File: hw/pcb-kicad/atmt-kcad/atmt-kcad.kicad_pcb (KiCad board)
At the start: 2 copper layers, 14 parts, among them J3 Conn_01x04_Male, J4 Conn_01x04_Male, U1 ESP32-WROOM-32U, U2 LP2987-3.3_SOIC8_VSSOP8, U3 4504, U4 L293

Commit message: Before refactoring
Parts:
- added C7: 100n, Capacitor_SMD:C_0805_2012Metric_Pad1.18x1.45mm_HandSolder, B.Cu at (101.2, 111.1)
- added D2: PowerOn, LED_THT:LED_D3.0mm, F.Cu at (94.7, 74.8)
- added J1: Reset, Connector_PinHeader_2.54mm:PinHeader_1x02_P2.54mm_Vertical, F.Cu at (111.2, 68.4)
- added J10: JTAG, Connector_PinHeader_2.54mm:PinHeader_1x04_P2.54mm_Vertical, F.Cu at (119.6, 68.4)
- added J11: BAT+, Connector_Wire:SolderWire-1.5sqmm_1x01_D1.7mm_OD3mm, F.Cu at (95.6, 106.4)
- added J12: BAT-, Connector_Wire:SolderWire-1.5sqmm_1x01_D1.7mm_OD3mm, F.Cu at (145.4, 72.8)
- added J13: Steering, Connector_Phoenix_MSTB:PhoenixContact_MSTBA_2,5_2-G-5,08_1x02_P5.08mm_Horizontal, F.Cu at (138.7, 75.6)
- added J14: Motor, Connector_Phoenix_MSTB:PhoenixContact_MSTBA_2,5_2-G-5,08_1x02_P5.08mm_Horizontal, F.Cu at (138.9, 116.4)
- added J15: BOOT, Connector_PinHeader_2.54mm:PinHeader_1x02_P2.54mm_Vertical, F.Cu at (111.2, 63.2)
- added J16: Light, Connector_PinHeader_2.54mm:PinHeader_1x03_P2.54mm_Vertical, F.Cu at (103.0, 82.0)
- added J17: Buck/Boost, Connector_PinHeader_2.54mm:PinHeader_1x03_P2.54mm_Vertical, F.Cu at (106.5, 119.5)
- added J2: PowerSw, Connector_PinHeader_2.54mm:PinHeader_1x02_P2.54mm_Vertical, F.Cu at (95.2, 112.4)
- added J5: US-Right, Connector_PinHeader_2.54mm:PinHeader_1x04_P2.54mm_Vertical, F.Cu at (144.8, 89.8)
- added J6: US-Left, Connector_PinHeader_2.54mm:PinHeader_1x04_P2.54mm_Vertical, F.Cu at (95.4, 89.8)
- added J7: I2Cx2, Connector_PinHeader_2.54mm:PinHeader_1x04_P2.54mm_Vertical, F.Cu at (119.5, 78.2)
- added J8: PRG, Connector_PinHeader_2.54mm:PinHeader_1x04_P2.54mm_Vertical, F.Cu at (119.5, 63.2)
- added J9: I2C_1, Connector_PinHeader_2.54mm:PinHeader_1x04_P2.54mm_Vertical, F.Cu at (119.5, 74.4)
- added R2: 10k, Resistor_SMD:R_0805_2012Metric_Pad1.20x1.40mm_HandSolder, B.Cu at (109.1, 87.3)
- added R3: 470k, Resistor_SMD:R_0805_2012Metric_Pad1.20x1.40mm_HandSolder, B.Cu at (101.1, 107.0)
- added R4: 100k, Resistor_SMD:R_0805_2012Metric_Pad1.20x1.40mm_HandSolder, B.Cu at (101.3, 115.1)
- added R5: 10k, Resistor_SMD:R_0805_2012Metric_Pad1.20x1.40mm_HandSolder, B.Cu at (121.0, 81.6)
- added R6: 10k, Resistor_SMD:R_0805_2012Metric_Pad1.20x1.40mm_HandSolder, B.Cu at (120.9, 85.1)
- added R7: 470, Resistor_SMD:R_0805_2012Metric_Pad1.20x1.40mm_HandSolder, B.Cu at (95.8, 78.4)
- C1, C4: value C -> 10u; moved to B.Cu
- C2: value C_Polarized -> 100n; footprint Capacitor_THT:CP_Axial_L11.0mm_D6.0mm_P18.00mm_Horizontal -> Capacitor_SMD:C_0805_2012Metric_Pad1.18x1.45mm_HandSolder; moved to B.Cu
- C3: value C -> 100n; moved to B.Cu
- C5: value C -> 1u; moved to B.Cu
- C6: value C_Polarized -> 22u
- D1, U3: moved to B.Cu
- J3: value Conn_01x04_Male -> US-Front
- J4: value Conn_01x04_Male -> US-Rear
- R1: value R -> 330k; moved to B.Cu
- U2: value LP2987-3.3_SOIC8_VSSOP8 -> LP2987-3.3; moved to B.Cu
- U4: value L293 -> L293DD; footprint Package_DIP:DIP-16_W7.62mm_SMDSocket_SmallPads -> MyFootprints:SO-20_STM; moved to B.Cu
- moved J3 171.7 mm to (101.4, 74.0), turned to 90 degrees
- moved J4 159.3 mm to (119.8, 119.6), turned to 90 degrees
- moved U4 107.8 mm to (135.1, 89.5), turned to 180 degrees
- moved C6 105.9 mm to (94.8, 82.4)
- moved U3 97.6 mm to (137.6, 105.9), turned to 180 degrees
- moved C2 90.8 mm to (112.6, 72.2)
- moved C4 90.8 mm to (108.7, 116.8)
- moved R1 75.9 mm to (105.0, 110.5), turned to -90 degrees
- moved C3 74.2 mm to (116.5, 87.7), turned to 90 degrees
- moved C1 72.1 mm to (114.1, 117.0), turned to 180 degrees
- moved C5 72.0 mm to (109.2, 91.4)
- moved U2 65.0 mm to (111.0, 110.6), turned to 180 degrees
- moved D1 33.4 mm to (111.1, 101.5)
- moved U1 17.0 mm to (121.8, 95.2)
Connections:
- C1 pad 1: unconnected-(C1-Pad1) -> GND
- C1 pad 2: unconnected-(C1-Pad2) -> B+
- C2 pad 1: unconnected-(C2-Pad1) -> /EN
- C2 pad 2: unconnected-(C2-Pad2) -> GND
- C3 pad 1: unconnected-(C3-Pad1) -> 3V3
- C3 pad 2: unconnected-(C3-Pad2) -> GND
- C4 pad 1: unconnected-(C4-Pad1) -> GND
- C4 pad 2: unconnected-(C4-Pad2) -> 3V3
- C5 pad 1: unconnected-(C5-Pad1) -> /EN
- C5 pad 2: unconnected-(C5-Pad2) -> GND
- C6 pad 1: unconnected-(C6-Pad1) -> 3V3
- C6 pad 2: unconnected-(C6-Pad2) -> GND
- D1 pad 1: unconnected-(D1-Pad1) -> Net-(D1-K)
- D1 pad 2: unconnected-(D1-Pad2) -> 3V3
- J3 pad 1: unconnected-(J3-Pad1) -> /5V
- J3 pad 2: unconnected-(J3-Pad2) -> /Trig1
- J3 pad 3: unconnected-(J3-Pad3) -> /Echo1
- J3 pad 4: unconnected-(J3-Pad4) -> GND
- J4 pad 1: unconnected-(J4-Pad1) -> /5V
- J4 pad 2: unconnected-(J4-Pad2) -> /Trig4
- J4 pad 3: unconnected-(J4-Pad3) -> /Echo4
- J4 pad 4: unconnected-(J4-Pad4) -> GND
- R1 pad 1: unconnected-(R1-Pad1) -> Net-(U2-~{ERROR})
- R1 pad 2: unconnected-(R1-Pad2) -> 3V3
- U1 pad 1: Net-(U1-Pad1) -> GND
- U1 pad 10: unconnected-(U1-Pad10) -> /Echo3L
- U1 pad 11: unconnected-(U1-Pad11) -> /Trig3
- U1 pad 12: unconnected-(U1-Pad12) -> /M2F
- U1 pad 13: unconnected-(U1-Pad13) -> /TMS
- U1 pad 14: unconnected-(U1-Pad14) -> /TDI
- U1 pad 15: Net-(U1-Pad1) -> GND
- U1 pad 16: unconnected-(U1-Pad16) -> /TCK
- U1 pad 2: unconnected-(U1-Pad2) -> 3V3
- U1 pad 23: unconnected-(U1-Pad23) -> /TDO
- U1 pad 24: unconnected-(U1-Pad24) -> /M1E
- U1 pad 25: unconnected-(U1-Pad25) -> /IO0
- U1 pad 26: unconnected-(U1-Pad26) -> /M1F
- U1 pad 27: unconnected-(U1-Pad27) -> /Trig1
- U1 pad 28: unconnected-(U1-Pad28) -> /Trig2
- U1 pad 29: unconnected-(U1-Pad29) -> /M1R
- U1 pad 3: unconnected-(U1-Pad3) -> /EN
- U1 pad 30: unconnected-(U1-Pad30) -> /Echo4L
- U1 pad 31: unconnected-(U1-Pad31) -> /Trig4
- U1 pad 33: unconnected-(U1-Pad33) -> /SDA
- U1 pad 34: unconnected-(U1-Pad34) -> /RX
- U1 pad 35: unconnected-(U1-Pad35) -> /TX
- U1 pad 36: unconnected-(U1-Pad36) -> /SCL
- U1 pad 37: unconnected-(U1-Pad37) -> /M2R
- U1 pad 38: Net-(U1-Pad1) -> GND
- U1 pad 39: Net-(U1-Pad1) -> GND
- U1 pad 6: unconnected-(U1-Pad6) -> /Echo1L
- U1 pad 7: unconnected-(U1-Pad7) -> /Echo2L
- U1 pad 8: unconnected-(U1-Pad8) -> /L1
- U1 pad 9: unconnected-(U1-Pad9) -> /M2E
- U2 pad 3: unconnected-(U2-Pad3) -> GND
- U2 pad 4: unconnected-(U2-Pad4) -> B+
- U2 pad 5: unconnected-(U2-Pad5) -> 3V3
- U2 pad 6: unconnected-(U2-Pad6) -> 3V3
- U2 pad 7: unconnected-(U2-Pad7) -> Net-(U2-~{ERROR})
- U2 pad 8: unconnected-(U2-Pad8) -> Net-(D1-K)
- U3 pad 1: unconnected-(U3-Pad1) -> /5V
- U3 pad 10: unconnected-(U3-Pad10) -> /Echo4L
- U3 pad 13: unconnected-(U3-Pad13) -> /5V
- U3 pad 16: unconnected-(U3-Pad16) -> 3V3
- U3 pad 2: unconnected-(U3-Pad2) -> /Echo1L
- U3 pad 3: unconnected-(U3-Pad3) -> /Echo1
- U3 pad 4: unconnected-(U3-Pad4) -> /Echo2L
- U3 pad 5: unconnected-(U3-Pad5) -> /Echo2
- U3 pad 6: unconnected-(U3-Pad6) -> /Echo3L
- U3 pad 7: unconnected-(U3-Pad7) -> /Echo3
- U3 pad 8: unconnected-(U3-Pad8) -> GND
- U3 pad 9: unconnected-(U3-Pad9) -> /Echo4
- U4 pad 1: unconnected-(U4-Pad1) -> /M1E
- U4 pad 10: unconnected-(U4-Pad10) -> /5V
- U4 pad 11: unconnected-(U4-Pad11) -> /M2E
- U4 pad 12: unconnected-(U4-Pad12) -> /M2F
- U4 pad 13: unconnected-(U4-Pad13) -> /M2_2
- U4 pad 14: unconnected-(U4-Pad14) -> GND
- U4 pad 15: unconnected-(U4-Pad15) -> GND
- U4 pad 16: unconnected-(U4-Pad16) -> GND
- U4 pad 2: unconnected-(U4-Pad2) -> /M1F
- U4 pad 3: unconnected-(U4-Pad3) -> /M1_1
- U4 pad 4: unconnected-(U4-Pad4) -> GND
- U4 pad 5: unconnected-(U4-Pad5) -> GND
- U4 pad 6: unconnected-(U4-Pad6) -> GND
- U4 pad 7: unconnected-(U4-Pad7) -> GND
- U4 pad 8: unconnected-(U4-Pad8) -> /M1_2
- U4 pad 9: unconnected-(U4-Pad9) -> /M1R
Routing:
- net /5V: track 0.00 -> 151.0 mm
- net /Echo3: track 0.00 -> 91.0 mm
- net /Echo1: track 0.00 -> 74.2 mm
- net 3V3: track 0.00 -> 70.2 mm
- net /M1_1: track 0.00 -> 46.2 mm
- net /RX: track 0.00 -> 40.8 mm
- net /TDI: track 0.00 -> 39.4 mm
- net /TCK: track 0.00 -> 39.4 mm
- net /TMS: track 0.00 -> 37.1 mm
- net /TDO: track 0.00 -> 36.7 mm
- net /SDA: track 0.00 -> 33.4 mm
- net /TX: track 0.00 -> 32.6 mm
- net /EN: track 0.00 -> 32.5 mm
- net B+: track 0.00 -> 32.4 mm
- net /Trig4: track 0.00 -> 27.6 mm
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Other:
- board outline added: 56 x 62.5 mm
- board text added: "3V3 GND RX TX"
- board text added: "3V3 GND SCL SDA"
- board text added: "5V TRIG ECHO GND"
- board text added: "A.T.M.T version 3 https://github.com/teddycool/atmt Pär Sundbäck 2024 par@sundback.com"
- board text added: "GND ECHO TRIG 5V"
- board text added: "GND L1 5V"
- board text added: "TMS TDI TCK TDO"

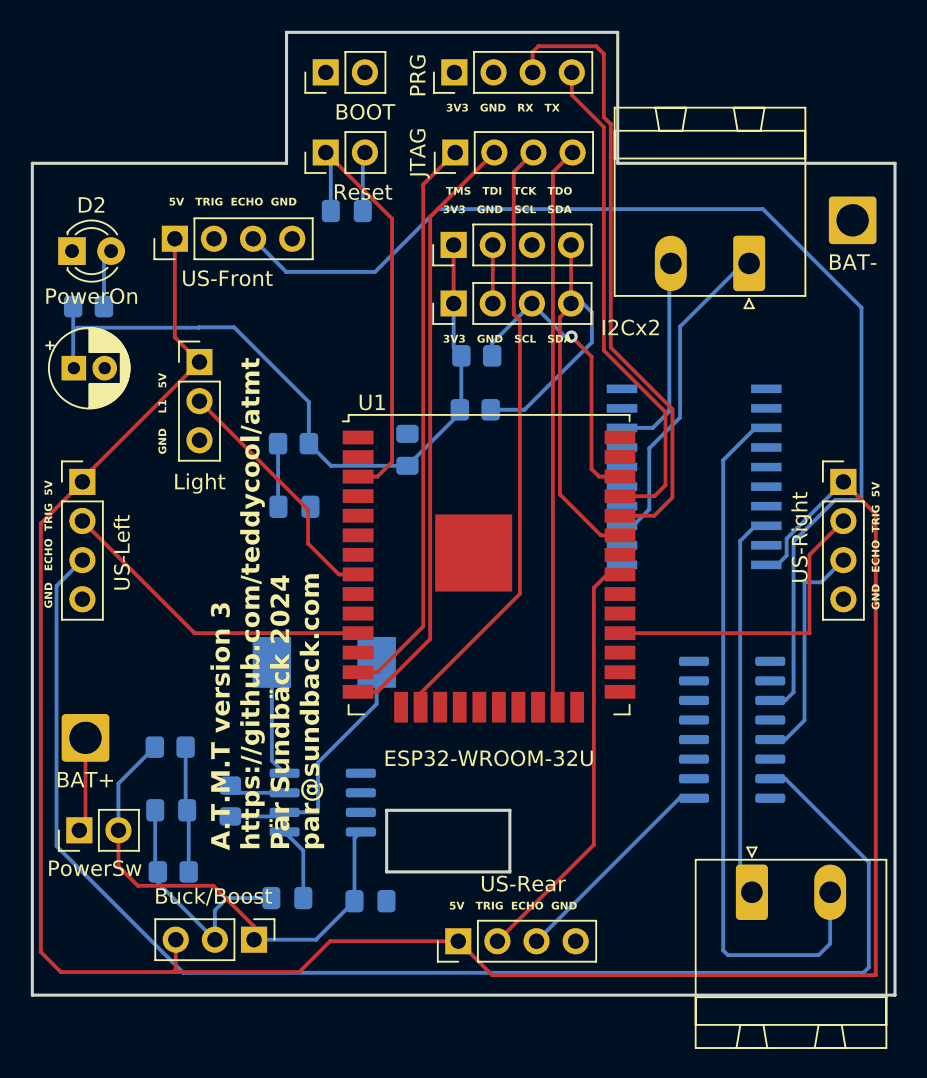
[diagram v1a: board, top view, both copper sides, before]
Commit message: added pin-descr
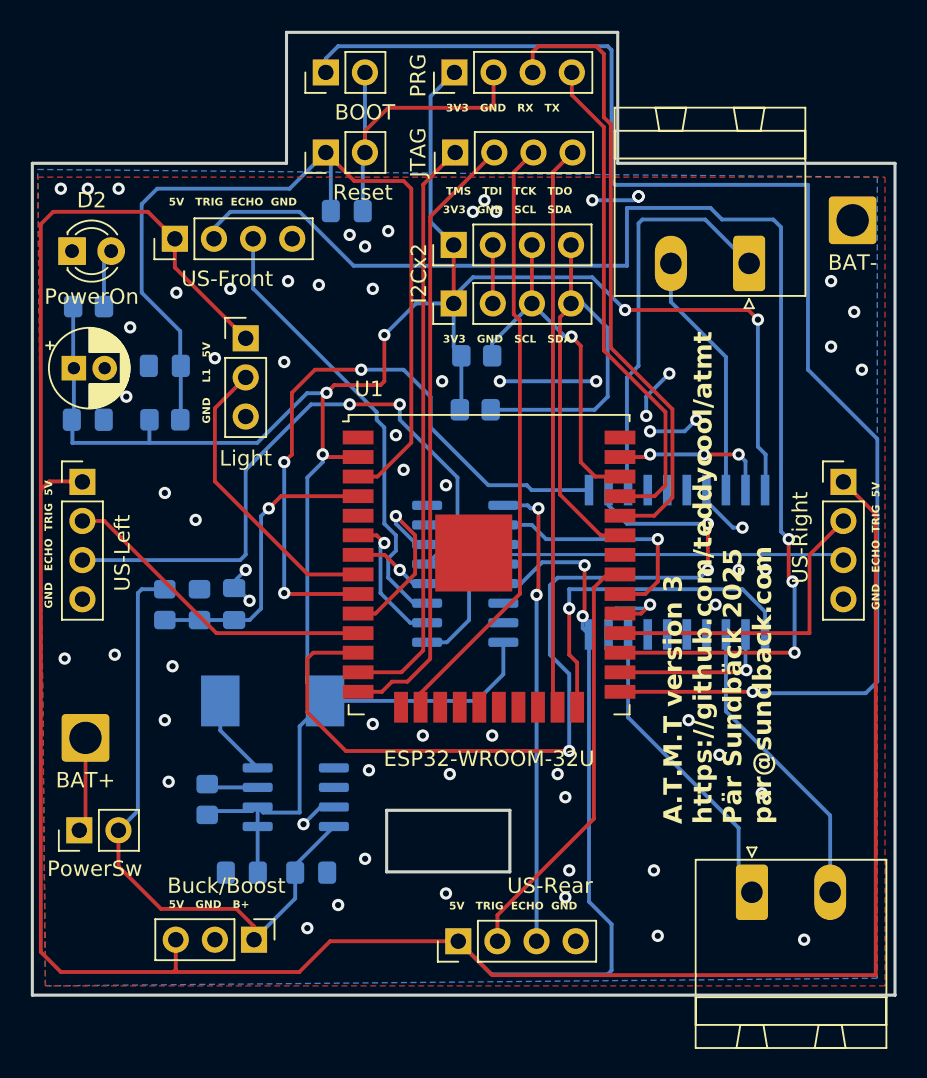
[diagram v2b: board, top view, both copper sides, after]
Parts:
- moved C3 20.8 mm to (95.8, 85.8), turned to 0 degrees
- moved U3 20.1 mm to (120.2, 95.8), turned to 0 degrees
- moved R4 17.4 mm to (103.0, 97.8), turned to 90 degrees
- moved C7 14.0 mm to (105.2, 97.7), turned to 90 degrees
- moved C5 12.4 mm to (100.8, 82.2), turned to 180 degrees
- moved R3 9.26 mm to (100.8, 97.8), turned to -90 degrees
- moved R2 8.49 mm to (100.8, 85.8), turned to 0 degrees
- moved U4 5.66 mm to (134.0, 95.0), turned to 90 degrees
- moved C1 4.27 mm to (110.2, 115.2)
- moved D1 4.18 mm to (107.8, 104.0)
- moved C4 3.38 mm to (105.8, 115.2)
- moved J16 3.37 mm to (106.0, 80.5)
- moved U2 1.78 mm to (109.2, 110.2)
- moved R1 1.50 mm to (103.5, 110.4)
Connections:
- U1 pad 4: unconnected-(U1-SENSOR_VP-Pad4) -> /ADC
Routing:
- net /IO0: track 0.00 -> 92.7 mm, vias 0 -> 1
- net 3V3: track 70.2 -> 153.8 mm, vias 0 -> 5
- net /Trig1: track 0.00 -> 83.1 mm, vias 0 -> 3
- net /5V: track 151.0 -> 212.2 mm, vias 0 -> 2
- net /M2F: track 0.00 -> 57.9 mm, vias 0 -> 3
- net /Echo3: track 91.0 -> 39.4 mm, vias 0 -> 2
- net /Echo1: track 74.2 -> 29.3 mm
- net /M2E: track 0.00 -> 42.3 mm, vias 0 -> 3
- net /EN: track 32.5 -> 59.7 mm
- net GND: track 23.6 -> 50.5 mm, vias 0 -> 68
- net /M1_1: track 46.2 -> 19.5 mm
- net /M1E: track 0.00 -> 22.7 mm, vias 0 -> 1
- net /Echo4: track 14.1 -> 30.7 mm, vias 0 -> 2
- net /Echo4L: track 0.00 -> 15.9 mm, vias 0 -> 1
- net /Echo2: track 14.8 -> 27.4 mm
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- added copper zone on B.Cu, net GND
- added copper zone on F.Cu, net GND
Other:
- board text added: "5V GND B+"
- board text added: "A.T.M.T version 3 https://github.com/teddycool/atmt Pär Sundbäck 2025 par@sundback.com"
- board text removed: "A.T.M.T version 3 https://github.com/teddycool/atmt Pär Sundbäck 2024 par@sundback.com"

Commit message: New kicad and a new hello-world-sw
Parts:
- added C8: 100n, Capacitor_SMD:C_0805_2012Metric_Pad1.18x1.45mm_HandSolder, B.Cu at (115.0, 107.5)
- U2: value LP2987-3.3 -> LP2988-3.3_SOIC8_VSSOP8
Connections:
- D1 pad 1: Net-(D1-K) -> B+
- U2 pad 1: unconnected-(U2-NC-Pad1) -> Net-(U2-BP)
- U2 pad 8: Net-(D1-K) -> B+
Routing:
- net B+: track 41.0 -> 51.7 mm
- net Net-(D1-K): track 5.35 -> 0.00 mm
- net Net-(U2-BP): track 0.00 -> 2.59 mm
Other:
- board text added: "A.T.M.T version 3.1 https://github.com/teddycool/atmt Pär Sundbäck 2025 par@sundback.com"
- board text removed: "A.T.M.T version 3 https://github.com/teddycool/atmt Pär Sundbäck 2025 par@sundback.com"
